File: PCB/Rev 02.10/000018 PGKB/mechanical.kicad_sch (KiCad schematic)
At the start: 14 parts

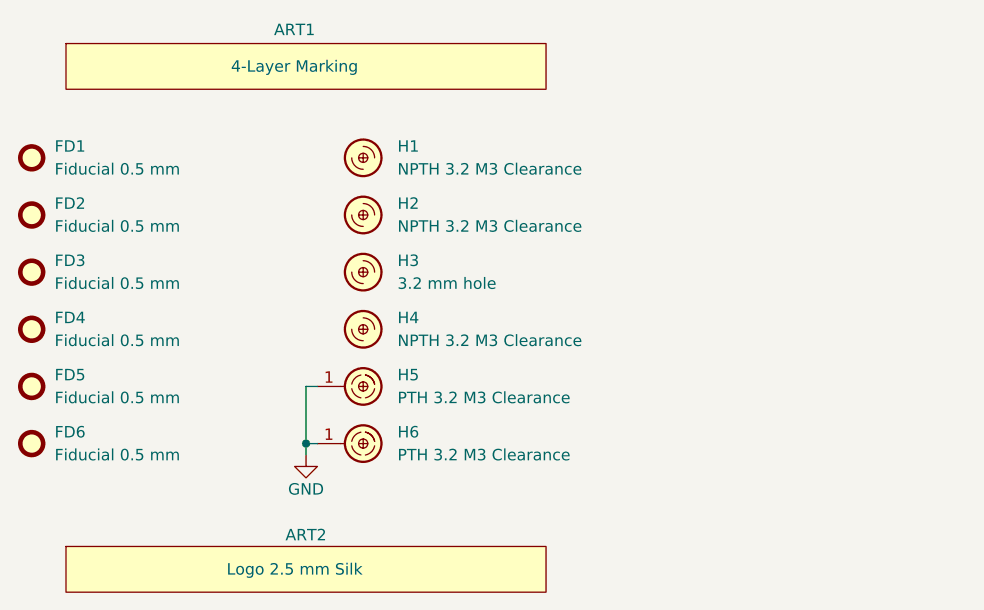
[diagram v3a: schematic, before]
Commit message: Resolved DRC problems
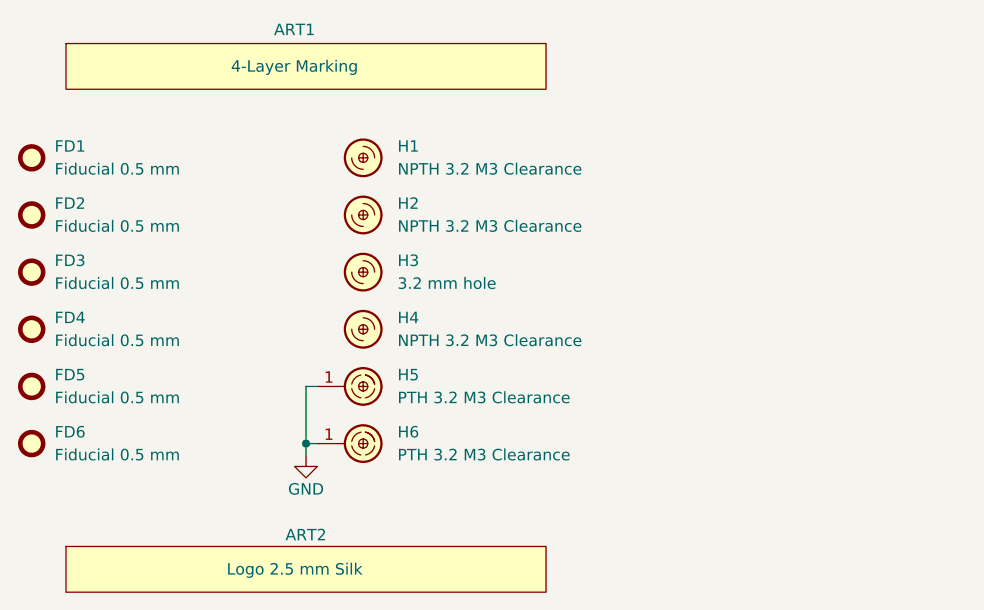
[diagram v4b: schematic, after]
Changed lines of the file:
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@@
 			)
 		)
-		(property "Description" ""
-			(at 154.94 64.77 0)
-			(effects
-				(font
-					(size 1.27 1.27)
-				)
+		(property "Description" "Artwork"
+			(at 142.494 33.274 0)
+			(effects
+				(font
+					(size 1.27 1.27)
+				)
+				(justify left)
 				(hide yes)
 			)
@@
 				)
 				(justify left)
+				(hide yes)
+			)
+		)
+		(property "Sim.Enable" "0"
+			(at 143.002 53.34 0)
+			(effects
+				(font
+					(size 1.27 1.27)
+				)
 				(hide yes)
 			)
@@
 		(fields_autoplaced yes)
 		(property "Reference" "H2"
-			(at 166.37 80.01 0)
+			(at 166.37 80.0099 0)
 			(effects
 				(font
@@
 		)
 		(property "Value" "NPTH 3.2 M3 Clearance"
-			(at 166.37 82.55 0)
+			(at 166.37 82.5499 0)
 			(effects
 				(font
@@
 			)
 		)
-		(property "Description" ""
+		(property "Description" "Hole"
 			(at 162.56 81.28 0)
 			(effects
@@
 		(fields_autoplaced yes)
 		(property "Reference" "FD2"
-			(at 128.27 80.01 0)
+			(at 128.27 80.0099 0)
 			(effects
 				(font
@@
 		)
 		(property "Value" "Fiducial 0.5 mm"
-			(at 128.27 82.55 0)
+			(at 128.27 82.5499 0)
 			(effects
 				(font
@@
 			)
 		)
-		(property "Description" ""
+		(property "Description" "Fiducial"
 			(at 125.73 81.28 0)
 			(effects
@@
 		(fields_autoplaced yes)
 		(property "Reference" "H6"
-			(at 166.37 105.41 0)
+			(at 166.37 105.4099 0)
 			(effects
 				(font
@@
 		)
 		(property "Value" "PTH 3.2 M3 Clearance"
-			(at 166.37 107.95 0)
+			(at 166.37 107.9499 0)
 			(effects
 				(font
@@
 			)
 		)
-		(property "Description" ""
+		(property "Description" "Hole"
 			(at 162.56 106.68 0)
 			(effects
@@
 		(fields_autoplaced yes)
 		(property "Reference" "FD4"
-			(at 128.27 92.71 0)
+			(at 128.27 92.7099 0)
 			(effects
 				(font
@@
 		)
 		(property "Value" "Fiducial 0.5 mm"
-			(at 128.27 95.25 0)
+			(at 128.27 95.2499 0)
 			(effects
 				(font
@@
 			)
 		)
-		(property "Description" ""
+		(property "Description" "Fiducial"
 			(at 125.73 93.98 0)
 			(effects
@@
 		(fields_autoplaced yes)
 		(property "Reference" "H5"
-			(at 166.37 99.06 0)
+			(at 166.37 99.0599 0)
 			(effects
 				(font
@@
 		)
 		(property "Value" "PTH 3.2 M3 Clearance"
-			(at 166.37 101.6 0)
+			(at 166.37 101.5999 0)
 			(effects
 				(font
@@
 			)
 		)
-		(property "Description" ""
+		(property "Description" "Hole"
 			(at 162.56 100.33 0)
 			(effects
@@
 		(fields_autoplaced yes)
 		(property "Reference" "FD3"
-			(at 128.27 86.36 0)
+			(at 128.27 86.3599 0)
 			(effects
 				(font
@@
 		)
 		(property "Value" "Fiducial 0.5 mm"
-			(at 128.27 88.9 0)
+			(at 128.27 88.8999 0)
 			(effects
 				(font
@@
 			)
 		)
-		(property "Description" ""
+		(property "Description" "Fiducial"
 			(at 125.73 87.63 0)
 			(effects
@@
 		(fields_autoplaced yes)
 		(property "Reference" "H4"
-			(at 166.37 92.71 0)
+			(at 166.37 92.7099 0)
 			(effects
 				(font
@@
 		)
 		(property "Value" "NPTH 3.2 M3 Clearance"
-			(at 166.37 95.25 0)
+			(at 166.37 95.2499 0)
 			(effects
 				(font
@@
 			)
 		)
-		(property "Description" ""
+		(property "Description" "Hole"
 			(at 162.56 93.98 0)
 			(effects
@@
 			)
 		)
-		(property "Description" ""
+		(property "Description" "Artwork"
 			(at 154.94 120.65 0)
 			(effects
@@
 				)
 				(justify left)
+				(hide yes)
+			)
+		)
+		(property "Sim.Enable" "0"
+			(at 143.002 108.966 0)
+			(effects
+				(font
+					(size 1.27 1.27)
+				)
 				(hide yes)
 			)
@@
 		(fields_autoplaced yes)
 		(property "Reference" "H3"
-			(at 166.37 86.36 0)
+			(at 166.37 86.3599 0)
 			(effects
 				(font
@@
 			)
 		)
-		(property "Description" ""
+		(property "Description" "Hole"
 			(at 162.56 87.63 0)
 			(effects
@@
 		)
 		(property "Code" "3.2 mm hole"
-			(at 166.37 88.9 0)
+			(at 166.37 88.8999 0)
 			(effects
 				(font
@@
 			)
 		)
-		(property "Description" ""
+		(property "Description" "Power symbol creates a global label with name \"GND\" , ground"
 			(at 156.21 107.95 0)
 			(effects
@@
 		(fields_autoplaced yes)
 		(property "Reference" "H1"
-			(at 166.37 73.66 0)
+			(at 166.37 73.6599 0)
 			(effects
 				(font
@@
 		)
 		(property "Value" "NPTH 3.2 M3 Clearance"
-			(at 166.37 76.2 0)
+			(at 166.37 76.1999 0)
 			(effects
 				(font
@@
 			)
 		)
-		(property "Description" ""
+		(property "Description" "Hole"
 			(at 162.56 74.93 0)
 			(effects
@@
 		(fields_autoplaced yes)
 		(property "Reference" "FD6"
-			(at 128.27 105.41 0)
+			(at 128.27 105.4099 0)
 			(effects
 				(font
@@
 		)
 		(property "Value" "Fiducial 0.5 mm"
-			(at 128.27 107.95 0)
+			(at 128.27 107.9499 0)
 			(effects
 				(font
@@
 			)
 		)
-		(property "Description" ""
+		(property "Description" "Fiducial"
 			(at 125.73 106.68 0)
 			(effects
@@
 		(fields_autoplaced yes)
 		(property "Reference" "FD1"
-			(at 128.27 73.66 0)
+			(at 128.27 73.6599 0)
 			(effects
 				(font
@@
 		)
 		(property "Value" "Fiducial 0.5 mm"
-			(at 128.27 76.2 0)
+			(at 128.27 76.1999 0)
 			(effects
 				(font
@@
 			)
 		)
-		(property "Description" ""
+		(property "Description" "Fiducial"
 			(at 125.73 74.93 0)
 			(effects
@@
 		(fields_autoplaced yes)
 		(property "Reference" "FD5"
-			(at 128.27 99.06 0)
+			(at 128.27 99.0599 0)
 			(effects
 				(font
@@
 		)
 		(property "Value" "Fiducial 0.5 mm"
-			(at 128.27 101.6 0)
+			(at 128.27 101.5999 0)
 			(effects
 				(font
@@
 			)
 		)
-		(property "Description" ""
+		(property "Description" "Fiducial"
 			(at 125.73 100.33 0)
 			(effects

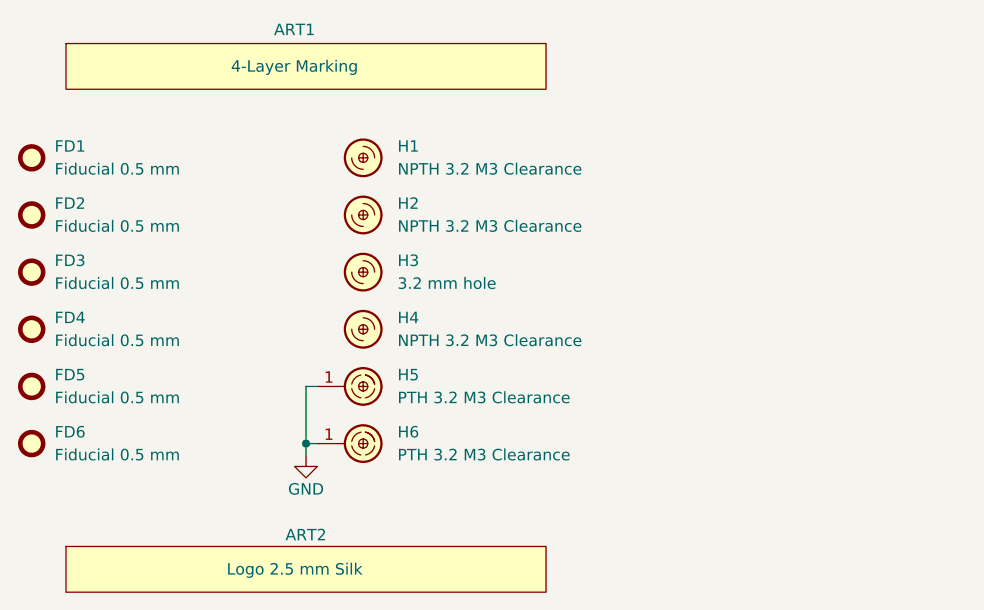
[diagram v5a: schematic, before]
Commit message: GND hook added
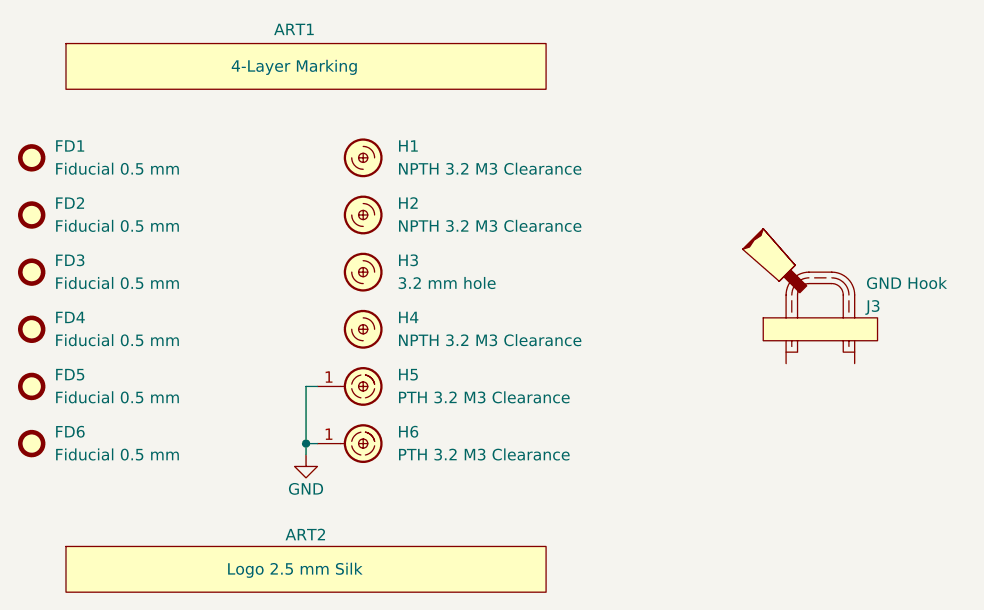
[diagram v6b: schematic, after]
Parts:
- added J3: GND Hook, KD_Connector_Pads:GND_HOOK_M, symbol KD_Connector_Pads:CON_GND_Probe_Hook
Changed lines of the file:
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@@
+	)
+	(symbol
+		(lib_id "KD_Connector_Pads:CON_GND_Probe_Hook")
+		(at 214.63 92.71 0)
+		(unit 1)
+		(exclude_from_sim no)
+		(in_bom yes)
+		(on_board yes)
+		(dnp no)
+		(fields_autoplaced yes)
+		(property "Reference" "J3"
+			(at 218.44 91.44 0)
+			(do_not_autoplace yes)
+			(effects
+				(font
+					(size 1.27 1.27)
+				)
+				(justify left)
+			)
+		)
+		(property "Value" "GND Hook"
+			(at 218.44 88.9 0)
+			(do_not_autoplace yes)
+			(effects
+				(font
+					(size 1.27 1.27)
+				)
+				(justify left)
+			)
+		)
+		(property "Footprint" "KD_Connector_Pads:GND_HOOK_M"
+			(at 201.93 78.74 0)
+			(effects
+				(font
+					(size 1.27 1.27)
+				)
+				(justify left)
+				(hide yes)
+			)
+		)
+		(property "Datasheet" ""
+			(at 201.93 81.28 0)
+			(effects
+				(font
+					(size 1.27 1.27)
+				)
+				(justify left)
+				(hide yes)
+			)
+		)
+		(property "Description" "Oscilloscope probe GND hook"
+			(at 201.93 60.96 0)
+			(effects
+				(font
+					(size 1.27 1.27)
+				)
+				(justify left)
+				(hide yes)
+			)
+		)
+		(property "Manufacturer" "DNP"
+			(at 201.93 63.5 0)
+			(effects
+				(font
+					(size 1.27 1.27)
+				)
+				(justify left)
+				(hide yes)
+			)
+		)
+		(property "MFG_PartNo" "DNP"
+			(at 201.93 66.04 0)
+			(effects
+				(font
+					(size 1.27 1.27)
+				)
+				(justify left)
+				(hide yes)
+			)
+		)
+		(property "Supplier" "DNP"
+			(at 201.93 68.58 0)
+			(effects
+				(font
+					(size 1.27 1.27)
+				)
+				(justify left)
+				(hide yes)
+			)
+		)
+		(property "Supplier_PartNo" "DNP"
+			(at 201.93 71.12 0)
+			(effects
+				(font
+					(size 1.27 1.27)
+				)
+				(justify left)
+				(hide yes)
+			)
+		)
+		(property "DNP" "T"
+			(at 201.93 73.66 0)
+			(effects
+				(font
+					(size 1.27 1.27)
+				)
+				(justify left)
+				(hide yes)
+			)
+		)
+		(property "Price" "0.00"
+			(at 201.93 76.2 0)
+			(effects
+				(font
+					(size 1.27 1.27)
+				)
+				(justify left)
+				(hide yes)
+			)
+		)
+		(pin "2"
+		)
+		(pin "1"
+		)
+		(instances
+			(project ""
+				(path "/e63e39d7-6ac0-4ffd-8aa3-1841a4541b55/8f5ee264-ab78-438d-b8d5-1e547e5afc7c"
+					(reference "J3")
+					(unit 1)
+				)
+			)
+		)
 	)
 	(symbol
